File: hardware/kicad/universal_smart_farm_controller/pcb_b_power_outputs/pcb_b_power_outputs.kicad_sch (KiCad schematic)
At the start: 55 parts, among them J1 Conn_01x12, J10 Conn_01x02, J11 Conn_01x02, J12 Conn_01x02, J13 Conn_01x02, J14 Conn_01x02, J15 Conn_01x02, J16 Conn_01x02, J17 Conn_01x02, J18 Conn_01x02, Q1 AO3400A, Q2 AO3400A, Q3 AO3400A, Q4 AO3400A, Q5 AO3400A, Q6 AO3400A, Q7 AO3400A, Q8 AO3400A

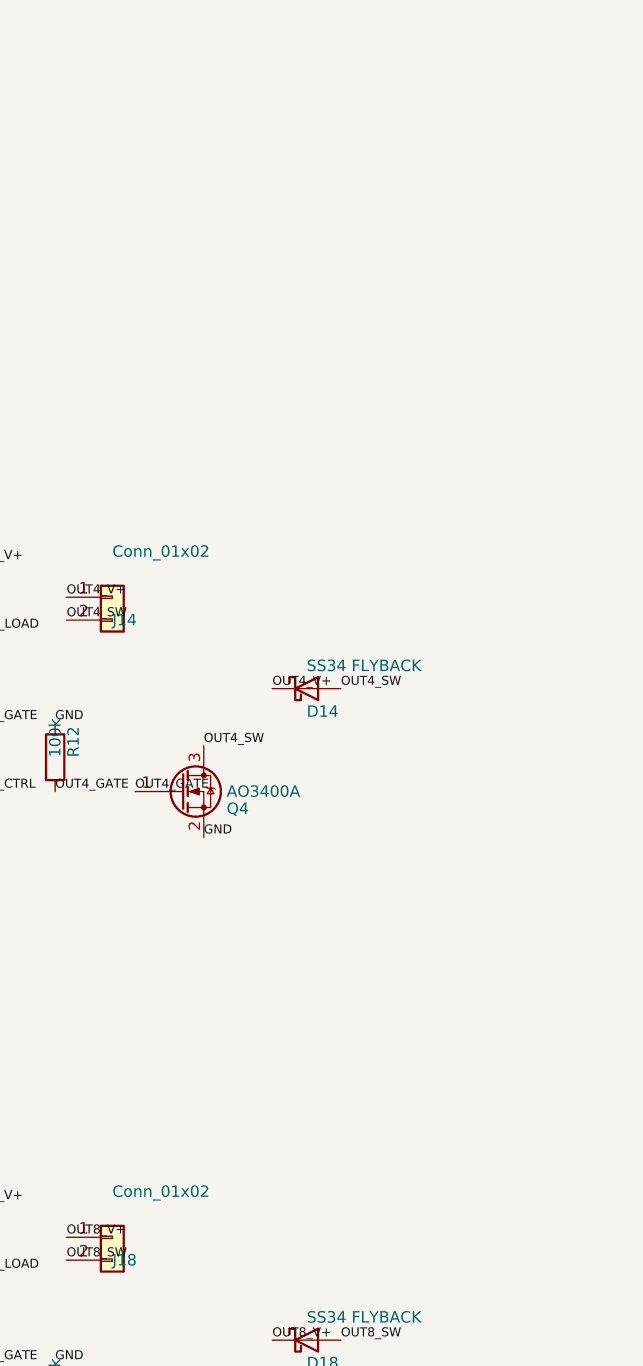
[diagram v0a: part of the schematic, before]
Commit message: Add supply and output LED circuits
Co-authored-by: tomnyle <175001228+tomnyle@users.noreply.github.com>
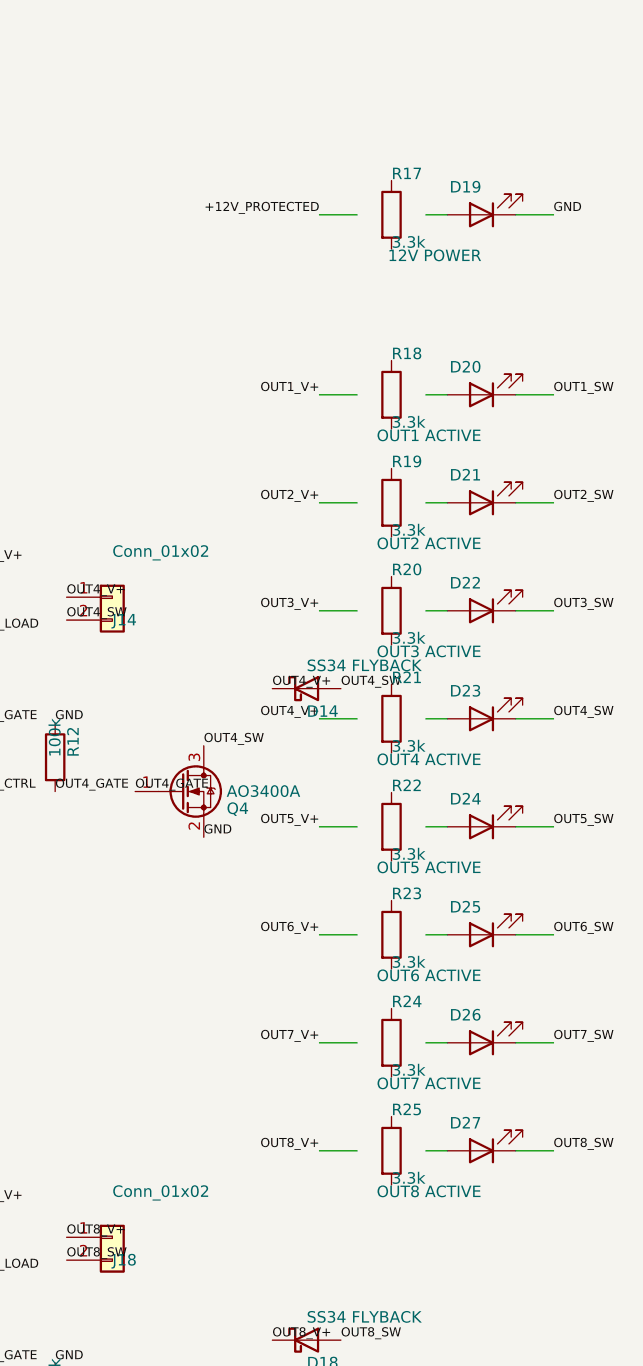
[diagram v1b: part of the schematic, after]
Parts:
- added D19: 12V POWER, LED_SMD:LED_0805_2012Metric, symbol Device:LED
- added D20: OUT1 ACTIVE, LED_SMD:LED_0805_2012Metric, symbol Device:LED
- added D21: OUT2 ACTIVE, LED_SMD:LED_0805_2012Metric, symbol Device:LED
- added D22: OUT3 ACTIVE, LED_SMD:LED_0805_2012Metric, symbol Device:LED
- added D23: OUT4 ACTIVE, LED_SMD:LED_0805_2012Metric, symbol Device:LED
- added D24: OUT5 ACTIVE, LED_SMD:LED_0805_2012Metric, symbol Device:LED
- added D25: OUT6 ACTIVE, LED_SMD:LED_0805_2012Metric, symbol Device:LED
- added D26: OUT7 ACTIVE, LED_SMD:LED_0805_2012Metric, symbol Device:LED
- added D27: OUT8 ACTIVE, LED_SMD:LED_0805_2012Metric, symbol Device:LED
- added R17, R18, R19, R20, R21, R22, R23, R24, R25: 3.3k, Resistor_SMD:R_0805_2012Metric, symbol Device:R
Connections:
- net GND: now also D19.1 (K)
- net OUT1_SW: now also D20.1 (K)
- net OUT2_SW: now also D21.1 (K)
- net OUT3_SW: now also D22.1 (K)
- net OUT4_SW: now also D23.1 (K)
- net OUT5_SW: now also D24.1 (K)
- net OUT6_SW: now also D25.1 (K)
- net OUT7_SW: now also D26.1 (K)
- net OUT8_SW: now also D27.1 (K)
